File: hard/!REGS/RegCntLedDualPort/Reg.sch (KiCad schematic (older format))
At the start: 42 parts, among them J1 Conn_01x08_Male, J10 Conn_01x01_Male, J11 Conn_01x08_Male, J2 Conn_01x08_Male, J3 Conn_01x02_Male, J4 Conn_01x03_Male, J5 Conn_01x02_Male, J6 Conn_01x02_Male, J7 Conn_01x01_Male, J8 Conn_01x01_Male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

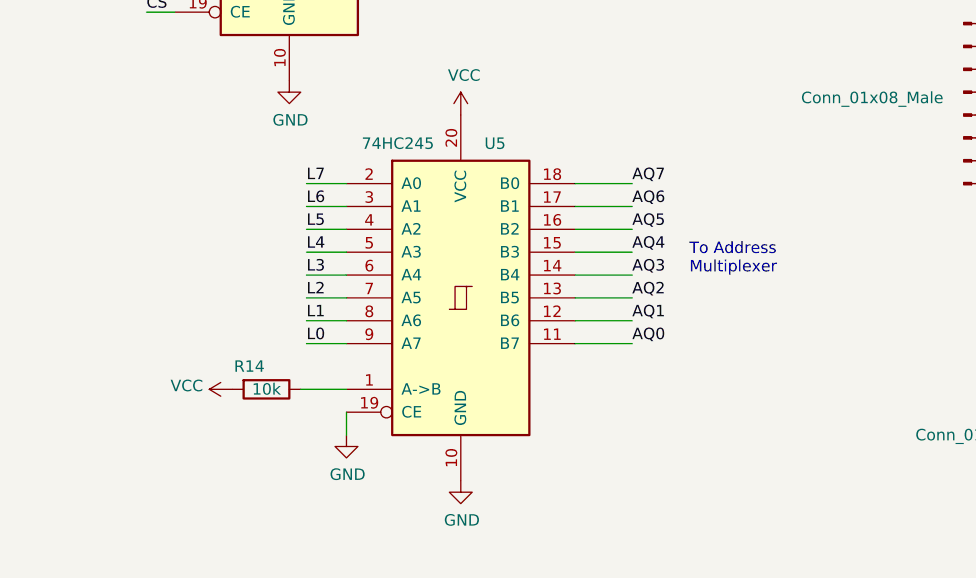
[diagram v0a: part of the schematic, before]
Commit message: RegCntLedDualPort is ready
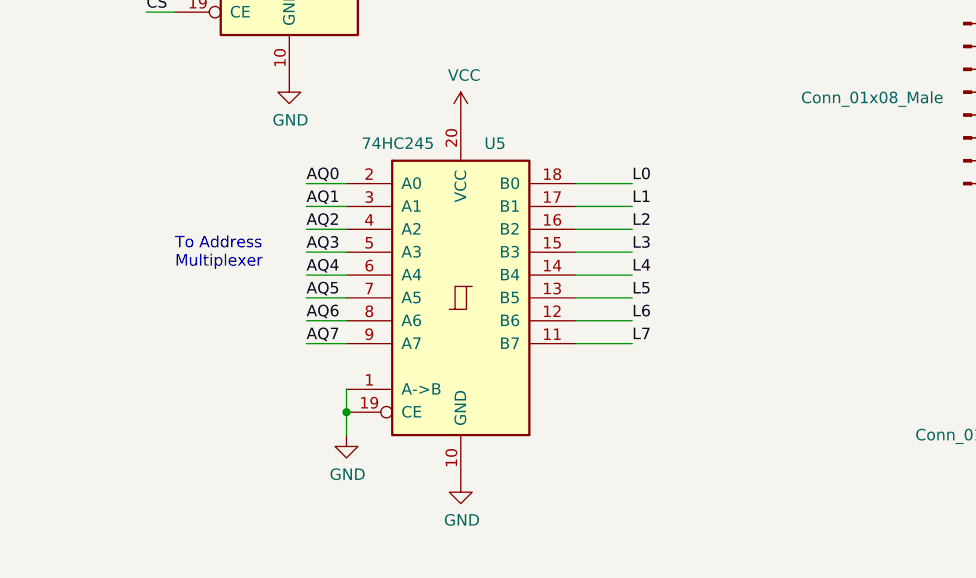
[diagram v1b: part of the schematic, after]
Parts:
- removed R14: 10k, Resistor_SMD:R_0805_2012Metric_Pad1.20x1.40mm_HandSolder, symbol Device:R
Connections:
- net AQ0: now also U5.2 (A0); no longer U5.11 (B7)
- net AQ1: now also U5.3 (A1); no longer U5.12 (B6)
- net AQ2: now also U5.4 (A2); no longer U5.13 (B5)
- net AQ3: now also U5.5 (A3); no longer U5.14 (B4)
- net AQ4: now also U5.6 (A4); no longer U5.15 (B3)
- net AQ5: now also U5.7 (A5); no longer U5.16 (B2)
- net AQ6: now also U5.8 (A6); no longer U5.17 (B1)
- net AQ7: now also U5.9 (A7); no longer U5.18 (B0)
- net GND: now also U5.1 (A->B)
- net L0: now also U5.18 (B0); no longer U5.9 (A7)
- net L1: now also U5.17 (B1); no longer U5.8 (A6)
- net L2: now also U5.16 (B2); no longer U5.7 (A5)
- net L3: now also U5.15 (B3); no longer U5.6 (A4)
- net L4: now also U5.14 (B4); no longer U5.5 (A3)
- net L5: now also U5.13 (B5); no longer U5.4 (A2)
- net L6: now also U5.12 (B6); no longer U5.3 (A1)
- net L7: now also U5.11 (B7); no longer U5.2 (A0)
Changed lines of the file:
@@
 Wire Wire Line
 	7550 3800 7300 3800
-Text Label 7550 3800 0    50   ~ 0
+Text Label 6125 3100 0    50   ~ 0
 AQ0
-Text Label 7550 3700 0    50   ~ 0
+Text Label 6125 3200 0    50   ~ 0
 AQ1
-Text Label 7550 3600 0    50   ~ 0
+Text Label 6125 3300 0    50   ~ 0
 AQ2
-Text Label 7550 3500 0    50   ~ 0
+Text Label 6125 3400 0    50   ~ 0
 AQ3
-Text Label 7550 3400 0    50   ~ 0
+Text Label 6125 3500 0    50   ~ 0
 AQ4
-Text Label 7550 3300 0    50   ~ 0
+Text Label 6125 3600 0    50   ~ 0
 AQ5
-Text Label 7550 3200 0    50   ~ 0
+Text Label 6125 3700 0    50   ~ 0
 AQ6
-Text Label 7550 3100 0    50   ~ 0
+Text Label 6125 3800 0    50   ~ 0
 AQ7
 $Comp
@@
 	1    0    0    -1
 $EndComp
-$Comp
-L Device:R R14
-U 1 1 65BD1D55
-P 5950 4000
-F 0 "R14" V 5850 3925 50  0000 C CNN
-F 1 "10k" V 5950 4000 50  0000 C CNN
-F 2 "Resistor_SMD:R_0805_2012Metric_Pad1.20x1.40mm_HandSolder" V 5880 4000 50  0001 C CNN
-F 3 "~" H 5950 4000 50  0001 C CNN
-	1    5950 4000
-	0    1    1    0
-$EndComp
-$Comp
-L power:VCC #PWR030
-U 1 1 65BD1D5B
-P 5800 4000
-F 0 "#PWR030" H 5800 3850 50  0001 C CNN
-F 1 "VCC" V 5815 4127 50  0000 L CNN
-F 2 "" H 5800 4000 50  0001 C CNN
-F 3 "" H 5800 4000 50  0001 C CNN
-	1    5800 4000
-	0    -1   -1   0
-$EndComp
-Wire Wire Line
-	6100 4000 6300 4000
-Text Label 6125 3800 0    50   ~ 0
+Text Label 7550 3100 0    50   ~ 0
 L0
-Text Label 6125 3700 0    50   ~ 0
+Text Label 7550 3200 0    50   ~ 0
 L1
-Text Label 6125 3600 0    50   ~ 0
+Text Label 7550 3300 0    50   ~ 0
 L2
-Text Label 6125 3500 0    50   ~ 0
+Text Label 7550 3400 0    50   ~ 0
 L3
-Text Label 6125 3400 0    50   ~ 0
+Text Label 7550 3500 0    50   ~ 0
 L4
-Text Label 6125 3300 0    50   ~ 0
+Text Label 7550 3600 0    50   ~ 0
 L5
-Text Label 6125 3200 0    50   ~ 0
+Text Label 7550 3700 0    50   ~ 0
 L6
-Text Label 6125 3100 0    50   ~ 0
+Text Label 7550 3800 0    50   ~ 0
 L7
 Wire Wire Line
@@
 Text Notes 7200 1700 0    50   ~ 0
 To Register\nMultiplexer
-Text Notes 7800 3500 0    50   ~ 0
+Text Notes 5550 3475 0    50   ~ 0
 To Address\nMultiplexer
 $Comp
@@
 	1    0    0    -1
 $EndComp
+Wire Wire Line
+	6300 4000 6300 4100
+Connection ~ 6300 4100
 $EndSCHEMATC
